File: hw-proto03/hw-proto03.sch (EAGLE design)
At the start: 30 parts, among them IC1 VN5E160MSTR-E, IC2 IR4427S, IC3 MCP2562T, IC5 IR4427S, J1 000, J2 000, J3 000, J4 000, Q1 SQJ147ELP-T1_GE3, Q2 SQJ147ELP-T1_GE3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

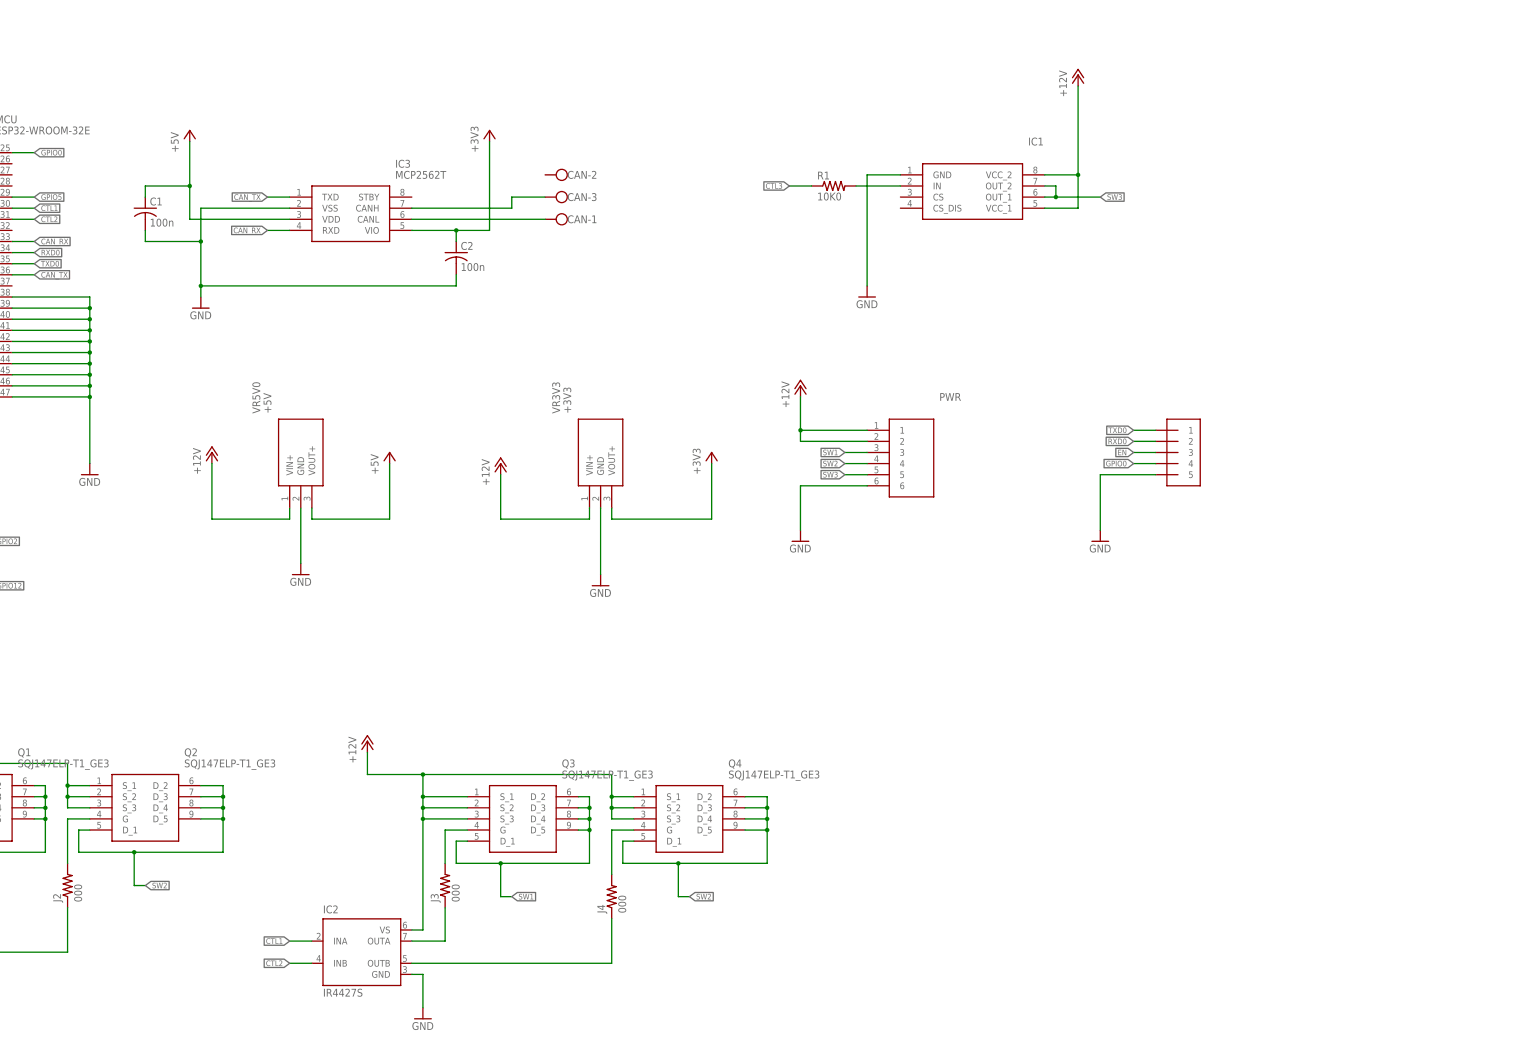
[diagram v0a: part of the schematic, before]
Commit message: big layout - 6 switches
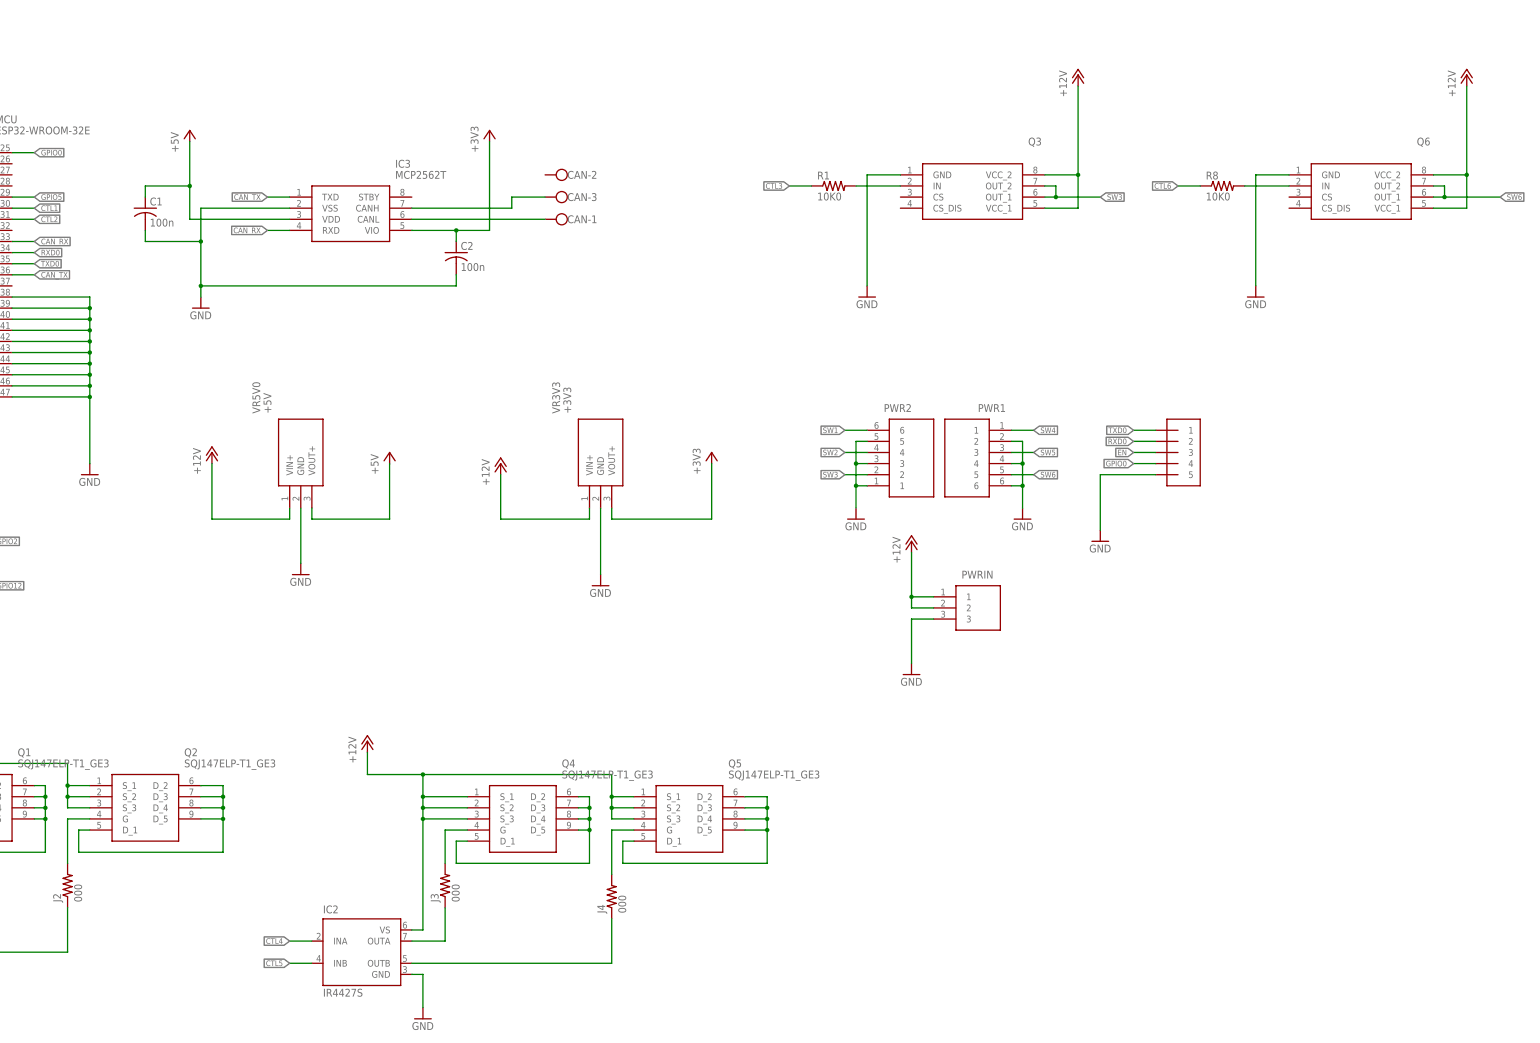
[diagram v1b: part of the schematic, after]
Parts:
- removed IC1: VN5E160MSTR-E, VN5E160MSTR-E:VN5E160MSTR-E
- removed PWR: 4DB-P108-06, 4DB-P108-06:4DB-P108-06
- added PWR1, PWR2: 4DB-P108-06, 4DB-P108-06:4DB-P108-06
- added PWRIN: 4DB-P108-03, con-barrier-3pos:4DB-P108-03
- added Q5: SQJ147ELP-T1_GE3, transistor-vishay-pchan-pso8:SQJ147ELP-T1_GE3
- added Q6: VN5E160MSTR-E, VN5E160MSTR-E:VN5E160MSTR-E
- added R8: 10K0, rcl:R-US_0204/7
- Q3: value SQJ147ELP-T1_GE3 -> VN5E160MSTR-E; device transistor-vishay-pchan-pso8:SQJ147ELP-T1_GE3 -> VN5E160MSTR-E:VN5E160MSTR-E
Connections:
- new net CTL5: IC2.INB
- new net CTL6: R8.1
- new net N$12: Q6.IN, R8.2
- new net SW4: PWR1.1, Q4.D_1, Q4.D_2, Q4.D_3, Q4.D_4, Q4.D_5
- new net SW5: PWR1.3, Q5.D_1, Q5.D_2, Q5.D_3, Q5.D_4, Q5.D_5
- new net SW6: PWR1.5, Q6.OUT_1, Q6.OUT_2
- net +12V: now also PWRIN.1, PWRIN.2, Q3.VCC_1, Q3.VCC_2, Q5.S_1, Q5.S_2, Q5.S_3, Q6.VCC_1, Q6.VCC_2; no longer IC1.VCC_1, IC1.VCC_2, PWR.1, PWR.2, Q3.S_1, Q3.S_2, Q3.S_3
- net CTL1: no longer IC2.INA
- net CTL2: no longer IC2.INB
- net CTL4: now also IC2.INA
- net GND: now also PWR1.2, PWR1.4, PWR1.6, PWR2.1, PWR2.3, PWR2.5, PWRIN.3, Q3.GND, Q6.GND; no longer IC1.GND, PWR.6
- net N$10: now also Q4.G; no longer Q3.G
- net N$11: now also Q5.G; no longer Q4.G
- net N$7: now also Q3.IN; no longer IC1.IN
- net SW1: now also PWR2.6; no longer PWR.3, Q3.D_1, Q3.D_2, Q3.D_3, Q3.D_4, Q3.D_5
- net SW2: now also PWR2.4; no longer PWR.4, Q4.D_1, Q4.D_2, Q4.D_3, Q4.D_4, Q4.D_5
- net SW3: now also PWR2.2, Q3.OUT_1, Q3.OUT_2; no longer IC1.OUT_1, IC1.OUT_2, PWR.5
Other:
- moved on the sheet: Q4

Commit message: layout continues
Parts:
- J1: value 000 -> J15MM; device rcl:R-US_0204/7 -> jumper:J15MM
- J2, J4: value 000 -> J5MM; device rcl:R-US_0204/7 -> jumper:J5MM
- J3: value 000 -> J12MM; device rcl:R-US_0204/7 -> jumper:J12MM
- R8: device rcl:R-US_0204/7 -> rcl:R-US_0207/12
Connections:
- removed net N$3: IC5.OUTB, J2.1
- new net N$13: IC5.OUTA, J2.1
- net CTL1: now also IC5.INB; no longer IC5.INA
- net CTL2: now also IC5.INA, MCU.IO4; no longer IC5.INB, MCU.IO19
- net CTL3: now also MCU.IO19; no longer MCU.IO27
- net CTL4: now also MCU.IO27; no longer MCU.IO26
- net CTL5: now also MCU.IO26
- net CTL6: now also MCU.IO25
- net N$4: now also IC5.OUTB; no longer IC5.OUTA
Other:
- moved on the sheet: Q3, Q6
